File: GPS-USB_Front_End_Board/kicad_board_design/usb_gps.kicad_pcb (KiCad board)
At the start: 4 copper layers, 99.1 x 53.3 mm, 86 parts, among them J1 Micro-USB Connector, J3 Edge Launch SMA, P1 CONN_02X12, U1 93LCxxB, U2 FT2232HL-REEL, U3 L4931 LDO, U4 MAX8510, U5 MAX8510, U6 MAX2769CETI+, U7 SAWTEK-855969, U8 LT1719S6 -- Not Populated, X1 13.368MHz TCXO, Y1 12MHz Crystal

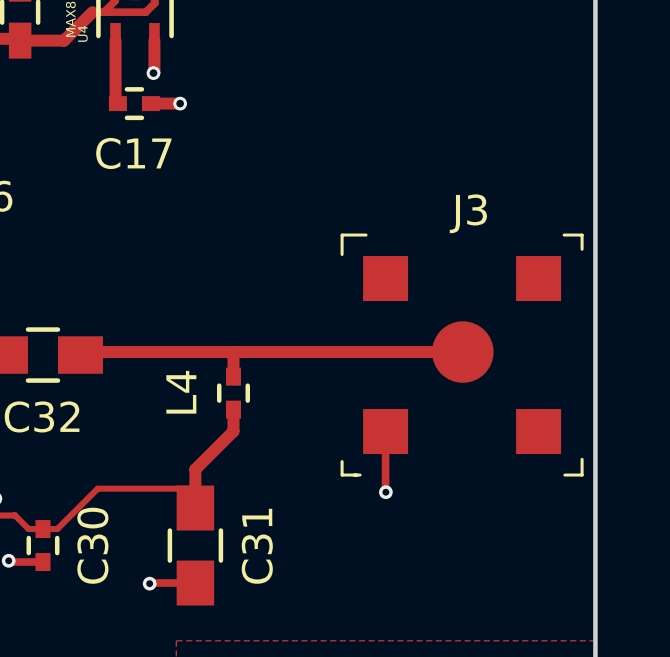
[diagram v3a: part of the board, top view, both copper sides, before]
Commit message: Change out SMA connector for thru-hole version.
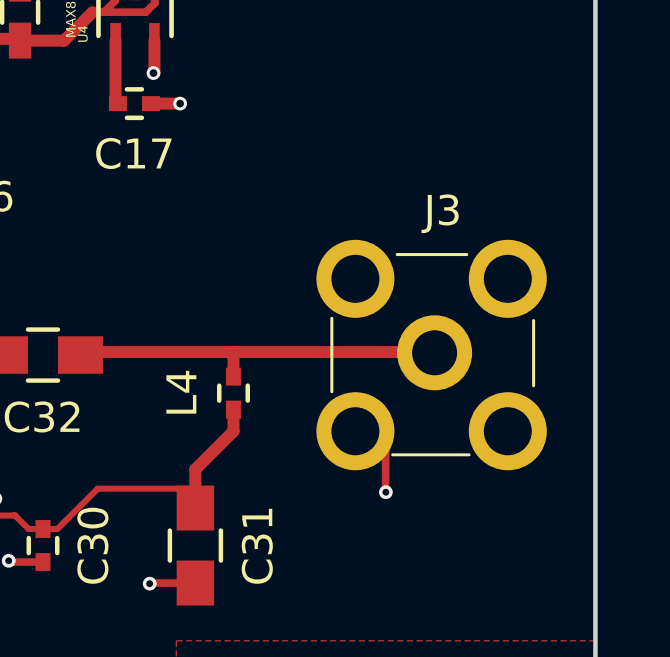
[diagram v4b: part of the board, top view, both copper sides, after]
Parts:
- J3: value Edge Launch SMA -> SMA; footprint digikey-footprints:RF_SMA_Receptical_Vertical_CONSMA001-SMD-G -> digikey-footprints:RF_SMA_Vertical_5-1814832-1
- moved J3 1.02 mm to (176.1, 81.9)
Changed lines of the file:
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@@
       (net 5 /MAX_2769/+5V))
-  )
-  (module digikey-footprints:RF_SMA_Receptical_Vertical_CONSMA001-SMD-G (layer F.Cu)
-    (at 177.165 81.915)
-    (fp_text reference J3 (at 0.3 -4.8) (layer F.SilkS)
-      (effects (font (size 1 1) (thickness 0.15)))
-    )
-    (fp_text value "Edge Launch SMA" (at 0.01778 5.15112) (layer F.Fab)
-      (effects (font (size 1 1) (thickness 0.15)))
-    )
-    (fp_text user %R (at -0.075 -2.675) (layer F.Fab)
-      (effects (font (size 0.75 0.75) (thickness 0.075)))
-    )
-    (fp_line (start -3.6 4) (end -3.4 4) (layer F.SilkS) (width 0.1))
-    (fp_line (start -3.5 4) (end -4 4) (layer F.SilkS) (width 0.1))
-    (fp_line (start -4 4) (end -4 3.55) (layer F.SilkS) (width 0.1))
-    (fp_line (start 4 3.475) (end 4 4) (layer F.SilkS) (width 0.1))
-    (fp_line (start 4 4) (end 3.425 4) (layer F.SilkS) (width 0.1))
-    (fp_line (start -3.2 -4) (end -4 -4) (layer F.SilkS) (width 0.1))
-    (fp_line (start -4 -4) (end -4 -3.35) (layer F.SilkS) (width 0.1))
-    (fp_line (start 3.4 -4) (end 4 -4) (layer F.SilkS) (width 0.1))
-    (fp_line (start 4 -4) (end 4 -3.525) (layer F.SilkS) (width 0.1))
-    (fp_line (start -4.13 4.13) (end -4.13 -4.13) (layer F.CrtYd) (width 0.05))
-    (fp_line (start 4.13 4.13) (end -4.13 4.13) (layer F.CrtYd) (width 0.05))
-    (fp_line (start 4.13 -4.13) (end 4.13 4.13) (layer F.CrtYd) (width 0.05))
-    (fp_line (start -4.13 -4.13) (end 4.13 -4.13) (layer F.CrtYd) (width 0.05))
-    (fp_line (start -3.88 -3.88) (end -3.88 3.88) (layer F.Fab) (width 0.1))
-    (fp_line (start 3.88 3.88) (end -3.88 3.88) (layer F.Fab) (width 0.1))
-    (fp_line (start 3.88 -3.88) (end 3.88 3.88) (layer F.Fab) (width 0.1))
-    (fp_line (start -3.88 -3.88) (end 3.88 -3.88) (layer F.Fab) (width 0.1))
-    (pad 1 smd rect (at -2.55 2.55) (size 1.5 1.5) (layers F.Cu F.Paste F.Mask)
-      (net 1 GND))
-    (pad 1 smd rect (at -2.55 -2.55) (size 1.5 1.5) (layers F.Cu F.Paste F.Mask)
-      (net 1 GND))
-    (pad 1 smd rect (at 2.55 -2.55) (size 1.5 1.5) (layers F.Cu F.Paste F.Mask)
-      (net 1 GND))
-    (pad 1 smd rect (at 2.55 2.55) (size 1.5 1.5) (layers F.Cu F.Paste F.Mask)
-      (net 1 GND))
-    (pad 2 smd circle (at 0.025 -0.1) (size 2.05 2.05) (layers F.Cu F.Paste F.Mask)
-      (net 18 "Net-(C32-Pad1)"))
   )
   (module Capacitors_SMD:C_0402 (layer F.Cu)
@@
     (pad 6 thru_hole oval (at 3.5 2.7 270) (size 1 1.55) (drill oval 0.5 1.15) (layers *.Cu *.Mask)
       (net 90 "Net-(C9-Pad1)"))
+  )
+  (module digikey-footprints:RF_SMA_Vertical_5-1814832-1 (layer F.Cu)
+    (at 176.149 81.915)
+    (fp_text reference J3 (at 0.375 -4.8) (layer F.SilkS)
+      (effects (font (size 1 1) (thickness 0.15)))
+    )
+    (fp_text value SMA (at 0.1 4.775) (layer F.Fab)
+      (effects (font (size 1 1) (thickness 0.15)))
+    )
+    (fp_line (start -1.3 3.325) (end 1.25 3.325) (layer F.SilkS) (width 0.1))
+    (fp_line (start -3.325 1.225) (end -3.325 -1.225) (layer F.SilkS) (width 0.1))
+    (fp_line (start 3.4 -1.15) (end 3.4 1.025) (layer F.SilkS) (width 0.1))
+    (fp_line (start -1.15 -3.35) (end 1.175 -3.35) (layer F.SilkS) (width 0.1))
+    (fp_line (start -4.1 4.1) (end -4.1 -4.1) (layer F.CrtYd) (width 0.05))
+    (fp_line (start 4.1 4.1) (end -4.1 4.1) (layer F.CrtYd) (width 0.05))
+    (fp_line (start 4.1 -4.1) (end 4.1 4.1) (layer F.CrtYd) (width 0.05))
+    (fp_line (start -4.1 -4.1) (end 4.1 -4.1) (layer F.CrtYd) (width 0.05))
+    (fp_line (start -3.2 3.2) (end -3.2 -3.2) (layer F.Fab) (width 0.1))
+    (fp_line (start 3.2 3.2) (end -3.2 3.2) (layer F.Fab) (width 0.1))
+    (fp_line (start 3.2 -3.2) (end 3.2 3.2) (layer F.Fab) (width 0.1))
+    (fp_line (start -3.2 -3.2) (end 3.2 -3.2) (layer F.Fab) (width 0.1))
+    (pad 2 thru_hole circle (at 0.1 -0.075) (size 2.5 2.5) (drill 1.5) (layers *.Cu *.Mask)
+      (net 18 "Net-(C32-Pad1)"))
+    (pad 1 thru_hole circle (at -2.54 -2.54) (size 2.6 2.6) (drill 1.6) (layers *.Cu *.Mask)
+      (net 1 GND))
+    (pad 1 thru_hole circle (at 2.54 -2.54) (size 2.6 2.6) (drill 1.6) (layers *.Cu *.Mask)
+      (net 1 GND))
+    (pad 1 thru_hole circle (at 2.54 2.54) (size 2.6 2.6) (drill 1.6) (layers *.Cu *.Mask)
+      (net 1 GND))
+    (pad 1 thru_hole circle (at -2.54 2.54) (size 2.6 2.6) (drill 1.6) (layers *.Cu *.Mask)
+      (net 1 GND))
   )
   (gr_text "GPS Front End\nUSB I/F" (at 174.625 94.742) (layer F.SilkS)
@@
   (segment (start 130.81 81.661) (end 129.159 81.661) (width 0.254) (layer F.Cu) (net 5))
   (segment (start 130.81 81.661) (end 130.81 82.55) (width 0.2032) (layer F.Cu) (net 5))
-  (segment (start 86.868 72.106) (end 88.676 72.106) (width 0.399999) (layer F.Cu) (net 6) (status 400000))
-  (segment (start 89.662 71.12) (end 90.89 71.12) (width 0.399999) (layer F.Cu) (net 6) (status 800000))
+  (segment (start 86.868 72.106) (end 88.676 72.106) (width 0.399999) (layer F.Cu) (net 6))
+  (segment (start 89.662 71.12) (end 90.89 71.12) (width 0.399999) (layer F.Cu) (net 6))
   (segment (start 88.676 72.106) (end 89.662 71.12) (width 0.399999) (layer F.Cu) (net 6))
   (segment (start 96.52 67.31) (end 96.52 65.024) (width 0.254) (layer F.Cu) (net 6) (status 20))
@@
   (segment (start 161.945 81.915) (end 161.945 82.022) (width 0.4) (layer F.Cu) (net 19))
   (segment (start 154.94 89.027) (end 154.94 90.33) (width 0.254) (layer F.Cu) (net 19))
-  (segment (start 94.996 72.71) (end 86.914 72.71) (width 0.399999) (layer F.Cu) (net 20) (status 800000))
-  (segment (start 86.914 72.71) (end 86.868 72.756) (width 0.399999) (layer F.Cu) (net 20) (status C00000))
+  (segment (start 94.996 72.71) (end 86.914 72.71) (width 0.399999) (layer F.Cu) (net 20))
+  (segment (start 86.914 72.71) (end 86.868 72.756) (width 0.399999) (layer F.Cu) (net 20))
   (segment (start 94.93 72.71) (end 94.996 72.71) (width 0.4) (layer F.Cu) (net 20))
   (segment (start 94.996 72.71) (end 96.64 72.71) (width 0.4) (layer F.Cu) (net 20))
-  (segment (start 86.868 73.406) (end 93.853 73.406) (width 0.399999) (layer F.Cu) (net 21) (status 400000))
-  (segment (start 95.057 74.61) (end 96.64 74.61) (width 0.399999) (layer F.Cu) (net 21) (status 800000))
+  (segment (start 86.868 73.406) (end 93.853 73.406) (width 0.399999) (layer F.Cu) (net 21))
+  (segment (start 95.057 74.61) (end 96.64 74.61) (width 0.399999) (layer F.Cu) (net 21))
   (segment (start 93.853 73.406) (end 95.057 74.61) (width 0.399999) (layer F.Cu) (net 21))
   (segment (start 96.574 74.676) (end 96.64 74.61) (width 0.4) (layer F.Cu) (net 21))
@@
   (segment (start 106.463 72.3) (end 107.315 72.3) (width 0.4) (layer F.Cu) (net 89))
   (segment (start 107.315 72.3) (end 106.463 72.3) (width 0.4) (layer F.Cu) (net 89))
-  (segment (start 84.168 76.906) (end 85.868 76.906) (width 0.399999) (layer F.Cu) (net 90) (status 400000))
-  (segment (start 85.868 76.906) (end 86.868 75.906) (width 0.399999) (layer F.Cu) (net 90) (status 800000))
-  (segment (start 84.168 69.906) (end 84.168 76.906) (width 0.399999) (layer F.Cu) (net 90) (status C00000))
-  (segment (start 86.868 70.906) (end 85.168 70.906) (width 0.399999) (layer F.Cu) (net 90) (status 400000))
-  (segment (start 85.168 70.906) (end 84.168 69.906) (width 0.399999) (layer F.Cu) (net 90) (status 800000))
-  (segment (start 91.567 66.844) (end 90.93 66.844) (width 0.399999) (layer F.Cu) (net 90) (status 400000))
-  (segment (start 90.93 66.844) (end 86.868 70.906) (width 0.399999) (layer F.Cu) (net 90) (status 800000))
+  (segment (start 84.168 76.906) (end 85.868 76.906) (width 0.399999) (layer F.Cu) (net 90))
+  (segment (start 85.868 76.906) (end 86.868 75.906) (width 0.399999) (layer F.Cu) (net 90))
+  (segment (start 84.168 69.906) (end 84.168 76.906) (width 0.399999) (layer F.Cu) (net 90))
+  (segment (start 86.868 70.906) (end 85.168 70.906) (width 0.399999) (layer F.Cu) (net 90))
+  (segment (start 85.168 70.906) (end 84.168 69.906) (width 0.399999) (layer F.Cu) (net 90))
+  (segment (start 91.567 66.844) (end 90.93 66.844) (width 0.399999) (layer F.Cu) (net 90))
+  (segment (start 90.93 66.844) (end 86.868 70.906) (width 0.399999) (layer F.Cu) (net 90))
   (segment (start 166.9097 71.4312) (end 166.9097 72.4853) (width 0.399999) (layer F.Cu) (net 91))
   (via (at 166.878 72.517) (size 0.4572) (drill 0.254) (layers F.Cu B.Cu) (net 91))

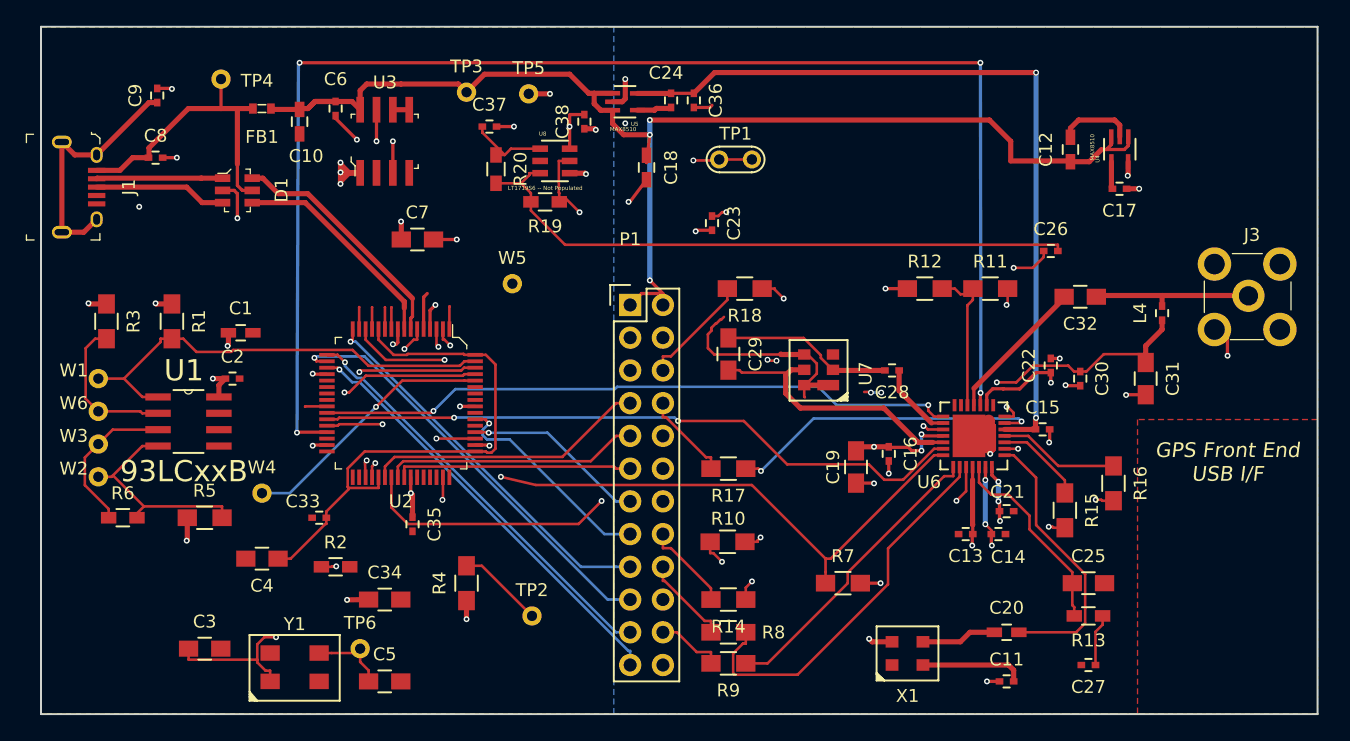
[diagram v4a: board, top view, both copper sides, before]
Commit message: Add back mounting holes, rev. front silk.
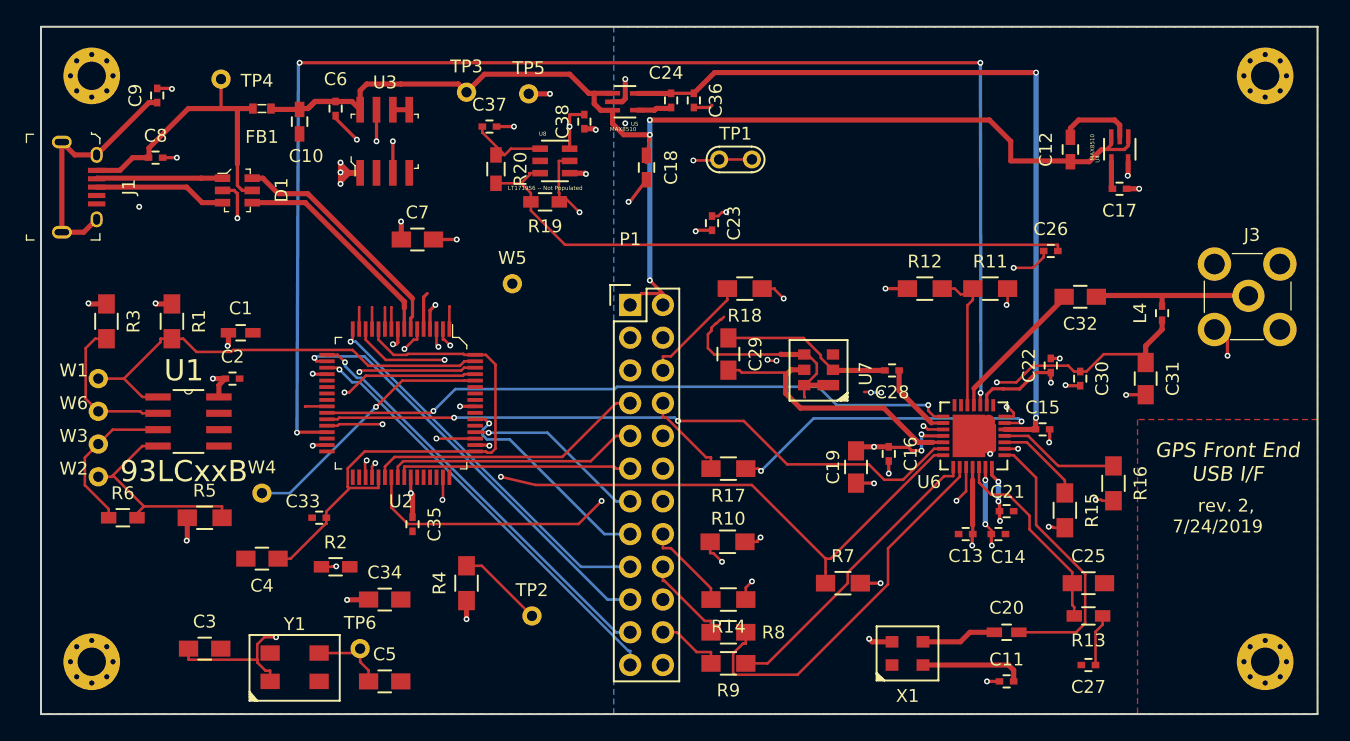
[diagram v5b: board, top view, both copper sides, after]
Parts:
- added REF**: MountingHole_2.2mm_M2_Pad_Via, Mounting_Holes:MountingHole_2.2mm_M2_Pad_Via, F.Cu at (86.5, 110.2)
- added REF**: MountingHole_2.2mm_M2_Pad_Via, Mounting_Holes:MountingHole_2.2mm_M2_Pad_Via, F.Cu at (177.5, 110.2)
- added REF**: MountingHole_2.2mm_M2_Pad_Via, Mounting_Holes:MountingHole_2.2mm_M2_Pad_Via, F.Cu at (177.5, 64.8)
- added REF**: MountingHole_2.2mm_M2_Pad_Via, Mounting_Holes:MountingHole_2.2mm_M2_Pad_Via, F.Cu at (86.5, 64.8)
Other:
- board text added: "rev. 2, 7/24/2019"
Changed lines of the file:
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@@
     (links 220)
     (no_connects 0)
-    (area 82.474999 60.884999 181.685001 114.375001)
+    (area 78.693 60.884999 181.685001 115.135)
     (thickness 1.6)
-    (drawings 5)
+    (drawings 6)
     (tracks 960)
     (zones 0)
-    (modules 86)
+    (modules 90)
     (nets 97)
   )
@@
   )
   (setup
-    (last_trace_width 0.399999)
+    (last_trace_width 0.2032)
     (user_trace_width 0.254)
     (user_trace_width 0.399999)
@@
     (uvia_drill 0.254)
   )
+  (module Mounting_Holes:MountingHole_2.2mm_M2_Pad_Via (layer F.Cu)
+    (at 86.487 110.236)
+    (descr "Mounting Hole 2.2mm, M2")
+    (tags "mounting hole 2.2mm m2")
+    (fp_text reference REF** (at 0 -3.2) (layer F.SilkS) hide
+      (effects (font (size 1 1) (thickness 0.15)))
+    )
+    (fp_text value MountingHole_2.2mm_M2_Pad_Via (at 0 3.2) (layer F.Fab) hide
+      (effects (font (size 1 1) (thickness 0.15)))
+    )
+    (fp_circle (center 0 0) (end 2.2 0) (layer Cmts.User) (width 0.15))
+    (fp_circle (center 0 0) (end 2.45 0) (layer F.CrtYd) (width 0.05))
+    (pad 1 thru_hole circle (at 0 0) (size 4.4 4.4) (drill 2.2) (layers *.Cu *.Mask))
+    (pad "" thru_hole circle (at 1.65 0) (size 0.6 0.6) (drill 0.4) (layers *.Cu *.Mask))
+    (pad "" thru_hole circle (at 1.166726 1.166726) (size 0.6 0.6) (drill 0.4) (layers *.Cu *.Mask))
+    (pad "" thru_hole circle (at 0 1.65) (size 0.6 0.6) (drill 0.4) (layers *.Cu *.Mask))
+    (pad "" thru_hole circle (at -1.166726 1.166726) (size 0.6 0.6) (drill 0.4) (layers *.Cu *.Mask))
+    (pad "" thru_hole circle (at -1.65 0) (size 0.6 0.6) (drill 0.4) (layers *.Cu *.Mask))
+    (pad "" thru_hole circle (at -1.166726 -1.166726) (size 0.6 0.6) (drill 0.4) (layers *.Cu *.Mask))
+    (pad "" thru_hole circle (at 0 -1.65) (size 0.6 0.6) (drill 0.4) (layers *.Cu *.Mask))
+    (pad "" thru_hole circle (at 1.166726 -1.166726) (size 0.6 0.6) (drill 0.4) (layers *.Cu *.Mask))
+  )
+  (module Mounting_Holes:MountingHole_2.2mm_M2_Pad_Via (layer F.Cu)
+    (at 177.546 110.236)
+    (descr "Mounting Hole 2.2mm, M2")
+    (tags "mounting hole 2.2mm m2")
+    (fp_text reference REF** (at 0 -3.2) (layer F.SilkS) hide
+      (effects (font (size 1 1) (thickness 0.15)))
+    )
+    (fp_text value MountingHole_2.2mm_M2_Pad_Via (at 0 3.2) (layer F.Fab) hide
+      (effects (font (size 1 1) (thickness 0.15)))
+    )
+    (fp_circle (center 0 0) (end 2.2 0) (layer Cmts.User) (width 0.15))
+    (fp_circle (center 0 0) (end 2.45 0) (layer F.CrtYd) (width 0.05))
+    (pad 1 thru_hole circle (at 0 0) (size 4.4 4.4) (drill 2.2) (layers *.Cu *.Mask))
+    (pad "" thru_hole circle (at 1.65 0) (size 0.6 0.6) (drill 0.4) (layers *.Cu *.Mask))
+    (pad "" thru_hole circle (at 1.166726 1.166726) (size 0.6 0.6) (drill 0.4) (layers *.Cu *.Mask))
+    (pad "" thru_hole circle (at 0 1.65) (size 0.6 0.6) (drill 0.4) (layers *.Cu *.Mask))
+    (pad "" thru_hole circle (at -1.166726 1.166726) (size 0.6 0.6) (drill 0.4) (layers *.Cu *.Mask))
+    (pad "" thru_hole circle (at -1.65 0) (size 0.6 0.6) (drill 0.4) (layers *.Cu *.Mask))
+    (pad "" thru_hole circle (at -1.166726 -1.166726) (size 0.6 0.6) (drill 0.4) (layers *.Cu *.Mask))
+    (pad "" thru_hole circle (at 0 -1.65) (size 0.6 0.6) (drill 0.4) (layers *.Cu *.Mask))
+    (pad "" thru_hole circle (at 1.166726 -1.166726) (size 0.6 0.6) (drill 0.4) (layers *.Cu *.Mask))
+  )
+  (module Mounting_Holes:MountingHole_2.2mm_M2_Pad_Via (layer F.Cu)
+    (at 177.546 64.77)
+    (descr "Mounting Hole 2.2mm, M2")
+    (tags "mounting hole 2.2mm m2")
+    (fp_text reference REF** (at 0 -3.2) (layer F.SilkS) hide
+      (effects (font (size 1 1) (thickness 0.15)))
+    )
+    (fp_text value MountingHole_2.2mm_M2_Pad_Via (at 0 3.2) (layer F.Fab) hide
+      (effects (font (size 1 1) (thickness 0.15)))
+    )
+    (fp_circle (center 0 0) (end 2.2 0) (layer Cmts.User) (width 0.15))
+    (fp_circle (center 0 0) (end 2.45 0) (layer F.CrtYd) (width 0.05))
+    (pad 1 thru_hole circle (at 0 0) (size 4.4 4.4) (drill 2.2) (layers *.Cu *.Mask))
+    (pad "" thru_hole circle (at 1.65 0) (size 0.6 0.6) (drill 0.4) (layers *.Cu *.Mask))
+    (pad "" thru_hole circle (at 1.166726 1.166726) (size 0.6 0.6) (drill 0.4) (layers *.Cu *.Mask))
+    (pad "" thru_hole circle (at 0 1.65) (size 0.6 0.6) (drill 0.4) (layers *.Cu *.Mask))
+    (pad "" thru_hole circle (at -1.166726 1.166726) (size 0.6 0.6) (drill 0.4) (layers *.Cu *.Mask))
+    (pad "" thru_hole circle (at -1.65 0) (size 0.6 0.6) (drill 0.4) (layers *.Cu *.Mask))
+    (pad "" thru_hole circle (at -1.166726 -1.166726) (size 0.6 0.6) (drill 0.4) (layers *.Cu *.Mask))
+    (pad "" thru_hole circle (at 0 -1.65) (size 0.6 0.6) (drill 0.4) (layers *.Cu *.Mask))
+    (pad "" thru_hole circle (at 1.166726 -1.166726) (size 0.6 0.6) (drill 0.4) (layers *.Cu *.Mask))
+  )
   (module Capacitors_SMD:C_0603_HandSoldering (layer F.Cu)
     (at 98.044 84.709)
@@
       (net 1 GND))
   )
+  (module Mounting_Holes:MountingHole_2.2mm_M2_Pad_Via (layer F.Cu)
+    (at 86.487 64.77)
+    (descr "Mounting Hole 2.2mm, M2")
+    (tags "mounting hole 2.2mm m2")
+    (fp_text reference REF** (at 0 -3.2) (layer F.SilkS) hide
+      (effects (font (size 1 1) (thickness 0.15)))
+    )
+    (fp_text value MountingHole_2.2mm_M2_Pad_Via (at 0 3.2) (layer F.Fab) hide
+      (effects (font (size 1 1) (thickness 0.15)))
+    )
+    (fp_circle (center 0 0) (end 2.2 0) (layer Cmts.User) (width 0.15))
+    (fp_circle (center 0 0) (end 2.45 0) (layer F.CrtYd) (width 0.05))
+    (pad 1 thru_hole circle (at 0 0) (size 4.4 4.4) (drill 2.2) (layers *.Cu *.Mask))
+    (pad "" thru_hole circle (at 1.65 0) (size 0.6 0.6) (drill 0.4) (layers *.Cu *.Mask))
+    (pad "" thru_hole circle (at 1.166726 1.166726) (size 0.6 0.6) (drill 0.4) (layers *.Cu *.Mask))
+    (pad "" thru_hole circle (at 0 1.65) (size 0.6 0.6) (drill 0.4) (layers *.Cu *.Mask))
+    (pad "" thru_hole circle (at -1.166726 1.166726) (size 0.6 0.6) (drill 0.4) (layers *.Cu *.Mask))
+    (pad "" thru_hole circle (at -1.65 0) (size 0.6 0.6) (drill 0.4) (layers *.Cu *.Mask))
+    (pad "" thru_hole circle (at -1.166726 -1.166726) (size 0.6 0.6) (drill 0.4) (layers *.Cu *.Mask))
+    (pad "" thru_hole circle (at 0 -1.65) (size 0.6 0.6) (drill 0.4) (layers *.Cu *.Mask))
+    (pad "" thru_hole circle (at 1.166726 -1.166726) (size 0.6 0.6) (drill 0.4) (layers *.Cu *.Mask))
+  )
+  (gr_text "   rev. 2, \n7/24/2019" (at 173.863 98.933) (layer F.SilkS)
+    (effects (font (size 1 1) (thickness 0.2)))
+  )
   (gr_text "GPS Front End\nUSB I/F" (at 174.625 94.742) (layer F.SilkS)
